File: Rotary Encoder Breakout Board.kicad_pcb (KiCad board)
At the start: 2 copper layers, 32 parts, among them J1 B5B-XH-A_LF__SN_, Q1 AO3401A, Q2 AO3401A, Q3 AO3401A, SW1 Rotary_Encoder_Switch, U1 SN74HC14DR

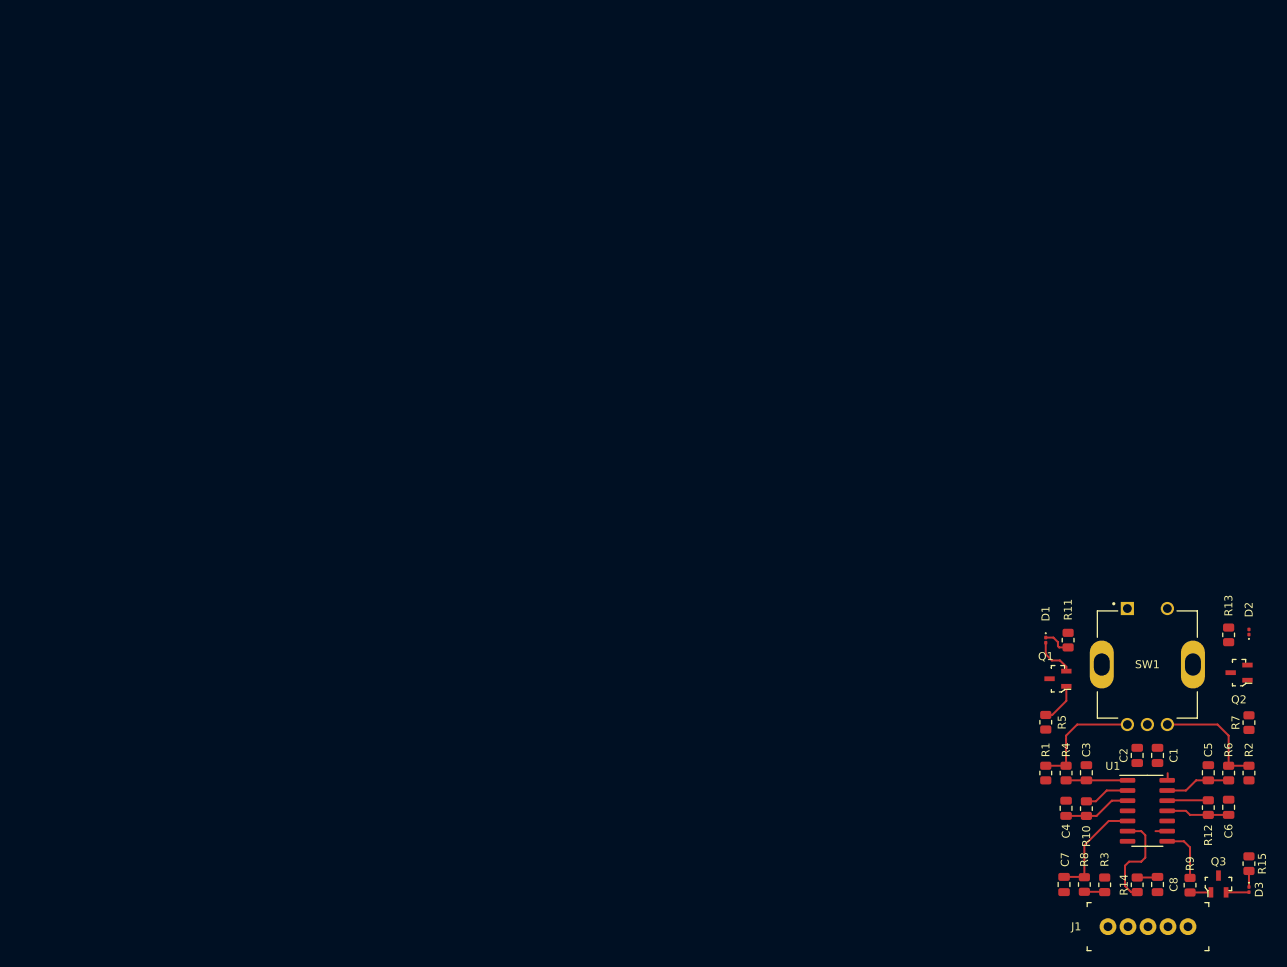
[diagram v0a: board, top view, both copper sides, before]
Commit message: simplified schematic + updated pcb + added pours, outline and mounting holes
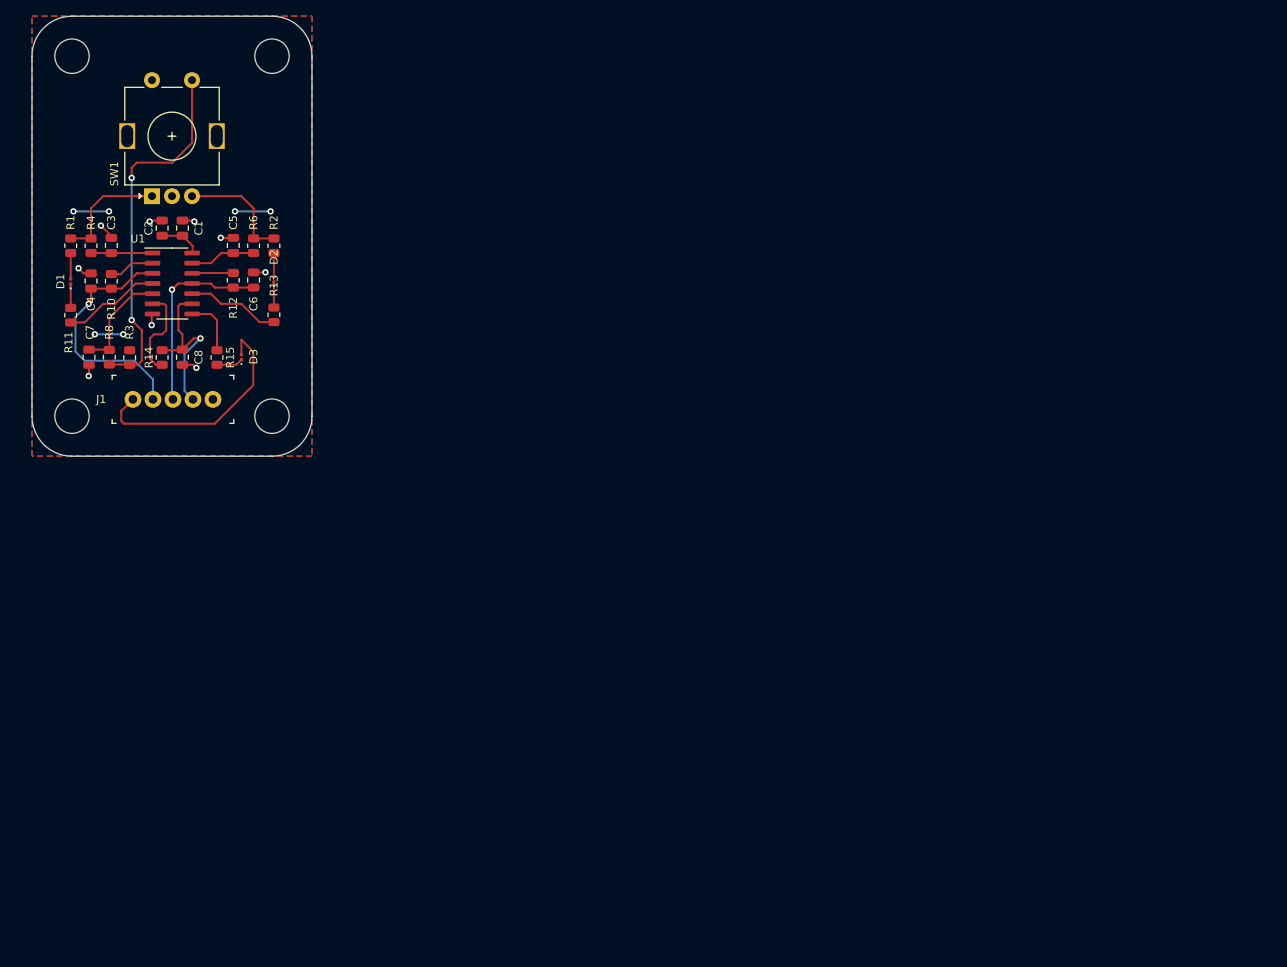
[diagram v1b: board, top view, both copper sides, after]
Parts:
- removed Q1, Q2, Q3: AO3401A, digikey-footprints:SOT-23-3
- removed R5, R7, R9: 510, Resistor_SMD:R_0805_2012Metric
- added H1: MountingHole, MountingHole:MountingHole_4.3mm_M4_ISO7380, F.Cu at (12.5, 35.0)
- added H2: MountingHole, MountingHole:MountingHole_4.3mm_M4_ISO7380, F.Cu at (-12.5, 35.0)
- added H3: MountingHole, MountingHole:MountingHole_4.3mm_M4_ISO7380, F.Cu at (12.5, -10.0)
- added H4: MountingHole, MountingHole:MountingHole_4.3mm_M4_ISO7380, F.Cu at (-12.5, -10.0)
- R11, R13, R15: value 1k8 -> 1k
- SW1: footprint SnapEDA:XDCR_PEC11R-4215F-S0024 -> Rotary_Encoder:RotaryEncoder_Alps_EC11E-Switch_Vertical_H20mm
- moved R15 143.7 mm to (5.63, 27.7)
- moved D3 142.4 mm to (8.67, 27.6), turned to 90 degrees
- moved C1 138.6 mm to (1.31, 11.5)
- moved C2 138.6 mm to (-1.23, 11.5)
- moved C3 138.6 mm to (-7.58, 13.7)
- moved C4 138.6 mm to (-10.1, 18.1)
- moved C6 138.6 mm to (10.2, 18.0)
- moved C7 138.6 mm to (-10.4, 27.6)
- moved C8 138.6 mm to (1.31, 27.6)
- moved J1 138.6 mm to (5.12, 32.9)
- moved R1 138.6 mm to (-12.7, 13.7)
- moved R10 138.6 mm to (-7.58, 18.1)
- moved R14 138.6 mm to (-1.23, 27.7)
- moved R2 138.6 mm to (12.7, 13.7)
- moved R3 138.6 mm to (-5.30, 27.7)
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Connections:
- D1 pad 2: Net-(D1-Pad2) -> VCC
- D2 pad 2: Net-(D2-Pad2) -> VCC
- D3 pad 2: Net-(D3-Pad2) -> VCC
- R11 pad 1: GND -> 2Y
- R13 pad 1: GND -> 5Y
- R15 pad 1: GND -> 4Y
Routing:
- net VCC: track 0.92 -> 54.0 mm, vias 0 -> 6
- net ROT_SW: track 2.56 -> 45.6 mm, vias 0 -> 2
- net 2A: track 8.47 -> 30.8 mm, vias 0 -> 1
- net 4A: track 4.03 -> 21.8 mm, vias 0 -> 1
- net 5A: track 7.90 -> 24.5 mm, vias 0 -> 1
- net GND: track 0.00 -> 14.9 mm, vias 0 -> 9
- net 2Y: track 0.00 -> 12.2 mm
- net 5Y: track 0.00 -> 11.7 mm
- net Net-(D1-Pad2): track 5.22 -> 0.00 mm
- net Net-(Q1-Pad1): track 5.12 -> 0.00 mm
- net Net-(D2-Pad1): track 0.00 -> 3.19 mm
- net Net-(D3-Pad2): track 2.87 -> 0.00 mm
- net Net-(Q3-Pad1): track 2.61 -> 0.00 mm
- net Net-(D3-Pad1): track 2.00 -> 3.31 mm
- net 3Y: track 12.6 -> 11.7 mm
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- added copper zone on B.Cu, net GND
- added copper zone on F.Cu, net VCC
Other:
- board outline added: 35 x 55 mm

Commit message: work in progress
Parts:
- J1: footprint digikey-footprints:PinHeader_1x5_P2.5mm_Drill1.1mm -> Connector_PinHeader_2.54mm:PinHeader_1x05_P2.54mm_Vertical
- moved J1 0.13 mm to (5.08, 33.0), turned to 270 degrees
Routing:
- net VCC: track 54.0 -> 23.9 mm
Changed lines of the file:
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@@
     (thickness 1.6)
     (drawings 8)
-    (tracks 151)
+    (tracks 143)
     (zones 0)
     (modules 30)
@@
     (mod_text_size 1 1)
     (mod_text_width 0.15)
-    (pad_size 1.524 1.524)
-    (pad_drill 0.762)
+    (pad_size 1.7 1.7)
+    (pad_drill 1)
     (pad_to_mask_clearance 0)
     (aux_axis_origin 0 0)
@@
     (add_net VCC)
   )
+  (module Connector_PinHeader_2.54mm:PinHeader_1x05_P2.54mm_Vertical (layer F.Cu)
+    (at 5.08 33.02 270)
+    (descr "Through hole straight pin header, 1x05, 2.54mm pitch, single row")
+    (tags "Through hole pin header THT 1x05 2.54mm single row")
+    (fp_text reference J1 (at 0 -2.33 90) (layer F.SilkS)
+      (effects (font (size 1 1) (thickness 0.15)))
+    )
+    (fp_text value B5B-XH-A_LF__SN_ (at 0 12.49 90) (layer F.Fab)
+      (effects (font (size 1 1) (thickness 0.15)))
+    )
+    (fp_text user %R (at 0 5.08) (layer F.Fab)
+      (effects (font (size 1 1) (thickness 0.15)))
+    )
+    (fp_line (start -0.635 -1.27) (end 1.27 -1.27) (layer F.Fab) (width 0.1))
+    (fp_line (start 1.27 -1.27) (end 1.27 11.43) (layer F.Fab) (width 0.1))
+    (fp_line (start 1.27 11.43) (end -1.27 11.43) (layer F.Fab) (width 0.1))
+    (fp_line (start -1.27 11.43) (end -1.27 -0.635) (layer F.Fab) (width 0.1))
+    (fp_line (start -1.27 -0.635) (end -0.635 -1.27) (layer F.Fab) (width 0.1))
+    (fp_line (start -1.33 11.49) (end 1.33 11.49) (layer F.SilkS) (width 0.12))
+    (fp_line (start -1.33 1.27) (end -1.33 11.49) (layer F.SilkS) (width 0.12))
+    (fp_line (start 1.33 1.27) (end 1.33 11.49) (layer F.SilkS) (width 0.12))
+    (fp_line (start -1.33 1.27) (end 1.33 1.27) (layer F.SilkS) (width 0.12))
+    (fp_line (start -1.33 0) (end -1.33 -1.33) (layer F.SilkS) (width 0.12))
+    (fp_line (start -1.33 -1.33) (end 0 -1.33) (layer F.SilkS) (width 0.12))
+    (fp_line (start -1.8 -1.8) (end -1.8 11.95) (layer F.CrtYd) (width 0.05))
+    (fp_line (start -1.8 11.95) (end 1.8 11.95) (layer F.CrtYd) (width 0.05))
+    (fp_line (start 1.8 11.95) (end 1.8 -1.8) (layer F.CrtYd) (width 0.05))
+    (fp_line (start 1.8 -1.8) (end -1.8 -1.8) (layer F.CrtYd) (width 0.05))
+    (pad 5 thru_hole oval (at 0 10.16 270) (size 1.7 1.7) (drill 1) (layers *.Cu *.Mask)
+      (net 2 VCC))
+    (pad 4 thru_hole oval (at 0 7.62 270) (size 1.7 1.7) (drill 1) (layers *.Cu *.Mask)
+      (net 4 2A))
+    (pad 3 thru_hole oval (at 0 5.08 270) (size 1.7 1.7) (drill 1) (layers *.Cu *.Mask)
+      (net 7 5A))
+    (pad 2 thru_hole oval (at 0 2.54 270) (size 1.7 1.7) (drill 1) (layers *.Cu *.Mask)
+      (net 6 4A))
+    (pad 1 thru_hole rect (at 0 0 270) (size 1.7 1.7) (drill 1) (layers *.Cu *.Mask)
+      (net 1 GND))
+    (model ${KISYS3DMOD}/Connector_PinHeader_2.54mm.3dshapes/PinHeader_1x05_P2.54mm_Vertical.wrl
+      (at (xyz 0 0 0))
+      (scale (xyz 1 1 1))
+      (rotate (xyz 0 0 0))
+    )
+  )
   (module MountingHole:MountingHole_4.3mm_M4_ISO7380 (layer F.Cu)
     (at -12.5 -10)
@@
     )
   )
-  (module digikey-footprints:PinHeader_1x5_P2.5mm_Drill1.1mm (layer F.Cu)
-    (at 5.1181 32.893 180)
-    (descr http://www.jst-mfg.com/product/pdf/eng/eXH.pdf)
-    (fp_text reference J1 (at 13.97 0) (layer F.SilkS)
-      (effects (font (size 1 1) (thickness 0.15)))
-    )
-    (fp_text value B5B-XH-A_LF__SN_ (at 5.1 4.2) (layer F.Fab) hide
-      (effects (font (size 1 1) (thickness 0.15)))
-    )
-    (fp_line (start -2.45 -2.875) (end -2.45 2.875) (layer F.Fab) (width 0.1))
-    (fp_line (start -2.45 -2.875) (end 12.45 -2.875) (layer F.Fab) (width 0.1))
-    (fp_line (start -2.6 3) (end -2.1 3) (layer F.SilkS) (width 0.1))
-    (fp_line (start -2.6 3) (end -2.6 2.5) (layer F.SilkS) (width 0.1))
-    (fp_line (start -2.6 -3) (end -2.1 -3) (layer F.SilkS) (width 0.1))
-    (fp_line (start -2.6 -3) (end -2.6 -2.5) (layer F.SilkS) (width 0.1))
-    (fp_line (start 12.7 -3.13) (end -2.7 -3.13) (layer F.CrtYd) (width 0.05))
-    (fp_line (start -2.7 -3.13) (end -2.7 3.12) (layer F.CrtYd) (width 0.05))
-    (fp_line (start 12.7 3.12) (end -2.7 3.12) (layer F.CrtYd) (width 0.05))
-    (fp_line (start -2.45 2.875) (end 12.45 2.875) (layer F.Fab) (width 0.1))
-    (fp_line (start 12.45 -2.875) (end 12.45 2.875) (layer F.Fab) (width 0.1))
-    (fp_line (start 12.7 -3.13) (end 12.7 3.12) (layer F.CrtYd) (width 0.05))
-    (fp_line (start 12.6 3) (end 12.6 2.5) (layer F.SilkS) (width 0.1))
-    (fp_line (start 12.6 3) (end 12.1 3) (layer F.SilkS) (width 0.1))
-    (fp_line (start 12.6 -3) (end 12.1 -3) (layer F.SilkS) (width 0.1))
-    (fp_line (start 12.6 -3) (end 12.6 -2.5) (layer F.SilkS) (width 0.1))
-    (fp_text user %R (at 3.556 -2.032) (layer F.Fab)
-      (effects (font (size 1 1) (thickness 0.15)))
-    )
-    (pad 5 thru_hole circle (at 10 0 180) (size 2.1 2.1) (drill 1.1) (layers *.Cu *.Mask)
-      (net 2 VCC))
-    (pad 4 thru_hole circle (at 7.5 0 180) (size 2.1 2.1) (drill 1.1) (layers *.Cu *.Mask)
-      (net 4 2A))
-    (pad 3 thru_hole circle (at 5 0 180) (size 2.1 2.1) (drill 1.1) (layers *.Cu *.Mask)
-      (net 7 5A))
-    (pad 2 thru_hole circle (at 2.5 0 180) (size 2.1 2.1) (drill 1.1) (layers *.Cu *.Mask)
-      (net 6 4A))
-    (pad 1 thru_hole circle (at 0 0 180) (size 2.1 2.1) (drill 1.1) (layers *.Cu *.Mask)
-      (net 1 GND))
-  )
   (module LED_SMD:LED_0201_0603Metric (layer F.Cu)
     (at 8.6741 27.625 90)
@@
     )
   )
+  (gr_line (start 12.5 40) (end -12.5 40) (layer Edge.Cuts) (width 0.05))
   (gr_arc (start -12.5 35) (end -17.5 35) (angle -90) (layer Edge.Cuts) (width 0.05))
   (gr_arc (start 12.5 35) (end 12.5 40) (angle -90) (layer Edge.Cuts) (width 0.05))
@@
   (gr_arc (start -12.5 -10) (end -12.5 -15) (angle -90) (layer Edge.Cuts) (width 0.05))
   (gr_line (start -17.5 35) (end -17.5 -10) (layer Edge.Cuts) (width 0.05))
-  (gr_line (start 12.5 40) (end -12.5 40) (layer Edge.Cuts) (width 0.05))
   (gr_line (start 17.5 -10) (end 17.5 35) (layer Edge.Cuts) (width 0.05))
   (gr_line (start -12.5 -15) (end 12.5 -15) (layer Edge.Cuts) (width 0.05))
@@
   (segment (start -7.874 9.398) (end -12.319 9.398) (width 0.25) (layer B.Cu) (net 2))
   (segment (start -9.652 24.765) (end -6.096 24.765) (width 0.25) (layer B.Cu) (net 2))
-  (segment (start -6.35 34.3611) (end -4.8819 32.893) (width 0.25) (layer F.Cu) (net 2))
-  (segment (start -6.35 35.56) (end -6.35 34.3611) (width 0.25) (layer F.Cu) (net 2))
-  (segment (start 5.334 35.941) (end -5.969 35.941) (width 0.25) (layer F.Cu) (net 2))
-  (segment (start 10.16 26.924) (end 10.16 31.115) (width 0.25) (layer F.Cu) (net 2))
-  (segment (start 10.16 31.115) (end 5.334 35.941) (width 0.25) (layer F.Cu) (net 2))
-  (segment (start 8.6741 25.4381) (end 10.16 26.924) (width 0.25) (layer F.Cu) (net 2))
-  (segment (start -5.969 35.941) (end -6.35 35.56) (width 0.25) (layer F.Cu) (net 2))
-  (segment (start 8.6741 27.305) (end 8.6741 25.4381) (width 0.25) (layer F.Cu) (net 2))
   (via (at 3.556 25.273) (size 0.8) (drill 0.4) (layers F.Cu B.Cu) (net 6))
   (via (at 0 19.177) (size 0.8) (drill 0.4) (layers F.Cu B.Cu) (net 7))
@@
   (segment (start -12.065 26.924) (end -10.922 28.067) (width 0.25) (layer B.Cu) (net 4))
   (segment (start -10.922 28.067) (end -4.699 28.067) (width 0.25) (layer B.Cu) (net 4))
-  (segment (start -2.3819 30.3841) (end -2.3819 32.893) (width 0.25) (layer B.Cu) (net 4))
-  (segment (start -4.699 28.067) (end -2.3819 30.3841) (width 0.25) (layer B.Cu) (net 4))
+  (segment (start -2.54 30.226) (end -4.699 28.067) (width 0.25) (layer B.Cu) (net 4))
+  (segment (start -2.54 33.02) (end -2.54 30.226) (width 0.25) (layer B.Cu) (net 4))
   (segment (start -7.8734 26.675) (end -7.8359 26.7125) (width 0.25) (layer F.Cu) (net 5))
   (segment (start -10.3759 26.675) (end -7.8734 26.675) (width 0.25) (layer F.Cu) (net 5))
@@
   (segment (start 1.0541 20.955) (end 0.8001 21.209) (width 0.25) (layer F.Cu) (net 6))
   (segment (start 2.5131 20.955) (end 1.0541 20.955) (width 0.25) (layer F.Cu) (net 6))
-  (segment (start 1.568101 27.260899) (end 3.556 25.273) (width 0.25) (layer B.Cu) (net 6))
-  (segment (start 1.568101 31.843001) (end 1.568101 27.260899) (width 0.25) (layer B.Cu) (net 6))
-  (segment (start 2.6181 32.893) (end 1.568101 31.843001) (width 0.25) (layer B.Cu) (net 6))
   (segment (start 2.7101 25.273) (end 1.3081 26.675) (width 0.25) (layer F.Cu) (net 6))
   (segment (start 3.556 25.273) (end 2.7101 25.273) (width 0.25) (layer F.Cu) (net 6))
+  (segment (start 1.568101 27.260899) (end 3.556 25.273) (width 0.25) (layer B.Cu) (net 6))
+  (segment (start 1.568101 32.048101) (end 1.568101 27.260899) (width 0.25) (layer B.Cu) (net 6))
+  (segment (start 2.54 33.02) (end 1.568101 32.048101) (width 0.25) (layer B.Cu) (net 6))
   (segment (start 10.1981 18.923) (end 7.6581 18.923) (width 0.25) (layer F.Cu) (net 7))
   (segment (start 7.6581 18.923) (end 5.3721 18.923) (width 0.25) (layer F.Cu) (net 7))
@@
   (segment (start 2.5131 18.415) (end 0.762 18.415) (width 0.25) (layer F.Cu) (net 7))
   (segment (start 0 32.7749) (end 0.1181 32.893) (width 0.25) (layer B.Cu) (net 7))
-  (segment (start 0 19.177) (end 0 32.7749) (width 0.25) (layer B.Cu) (net 7))
+  (segment (start 0 33.02) (end 0 19.177) (width 0.25) (layer B.Cu) (net 7))
   (segment (start 7.6581 14.605) (end 6.1341 14.605) (width 0.25) (layer F.Cu) (net 8))
   (segment (start 4.8641 15.875) (end 2.5131 15.875) (width 0.25) (layer F.Cu) (net 8))

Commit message: changed led footprint + added cast. holes + placed labels + pin header
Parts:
- added REF**: pad_castellated_pcbmount, tc-lib:pad_castellated_pcbmount, F.Cu at (-17.5, -2.50)
- added REF**: pad_castellated_pcbmount, tc-lib:pad_castellated_pcbmount, F.Cu at (17.5, -2.50)
- added REF**: pad_castellated_pcbmount, tc-lib:pad_castellated_pcbmount, F.Cu at (-17.5, 27.5)
- added REF**: pad_castellated_pcbmount, tc-lib:pad_castellated_pcbmount, F.Cu at (17.5, 27.5)
- added REF**: pad_castellated_P2.54, tc-lib:pad_castellated_P2.54, F.Cu at (5.08, 40.0)
- added REF**: pad_castellated_P2.54, tc-lib:pad_castellated_P2.54, F.Cu at (-5.08, 40.0)
- added REF**: pad_castellated_P2.54, tc-lib:pad_castellated_P2.54, F.Cu at (-2.54, 40.0)
- added REF**: pad_castellated_P2.54, tc-lib:pad_castellated_P2.54, F.Cu at (2.54, 40.0)
- added REF**: pad_castellated_P2.54, tc-lib:pad_castellated_P2.54, F.Cu at (0.00, 40.0)
- D1, D2, D3: footprint LED_SMD:LED_0201_0603Metric -> LED_SMD:LED_1206_3216Metric
- moved D1 1.31 mm to (-14.0, 18.2)
- moved D2 1.23 mm to (14.0, 17.9)
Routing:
- net 5A: track 24.7 -> 31.7 mm
- net 2A: track 30.8 -> 37.8 mm
- net GND: track 14.9 -> 21.8 mm
- net 4A: track 21.9 -> 28.8 mm
- net VCC: track 23.9 -> 29.8 mm
- net Net-(D2-Pad1): track 3.19 -> 2.62 mm
- net Net-(D1-Pad1): track 2.98 -> 2.44 mm

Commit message: added OSHW maker + designed with KiCAd + fiducials + license
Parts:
- added REF**: Fiducial_1mm_Mask2mm, Fiducial:Fiducial_1mm_Mask2mm, F.Cu at (-7.00, 37.0)
- added REF**: Fiducial_1mm_Mask2mm, Fiducial:Fiducial_1mm_Mask2mm, F.Cu at (14.0, 7.00)
- added REF**: Fiducial_1mm_Mask2mm, Fiducial:Fiducial_1mm_Mask2mm, F.Cu at (-6.00, -11.0)
- added REF**: OSHW-Logo2_7.3x6mm_Copper, Symbol:OSHW-Logo2_7.3x6mm_Copper, F.Cu at (0.02, -11.7)
- added REF**: KiCad-Logo2_5mm_SilkScreen, Symbol:KiCad-Logo2_5mm_SilkScreen, F.Cu at (-12.4, 1.84)
